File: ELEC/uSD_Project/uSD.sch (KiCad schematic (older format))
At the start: 5 parts, among them J1 CONN_01X08, U1 74HC595, U2 74HC165

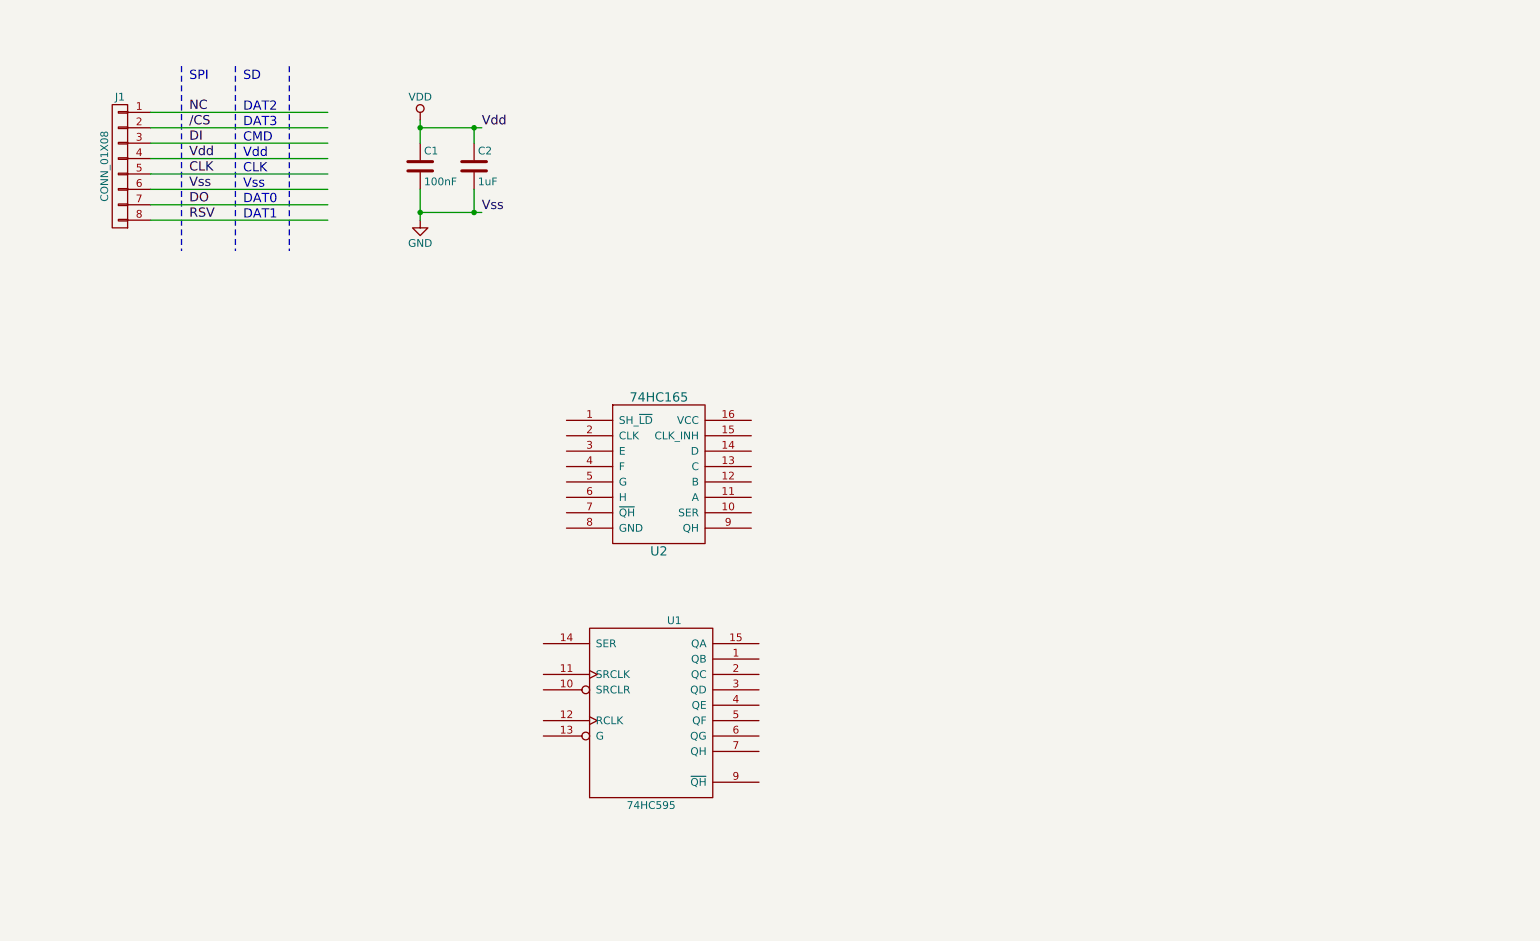
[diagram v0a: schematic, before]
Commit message: - Schematic capture - Creation of uSD part
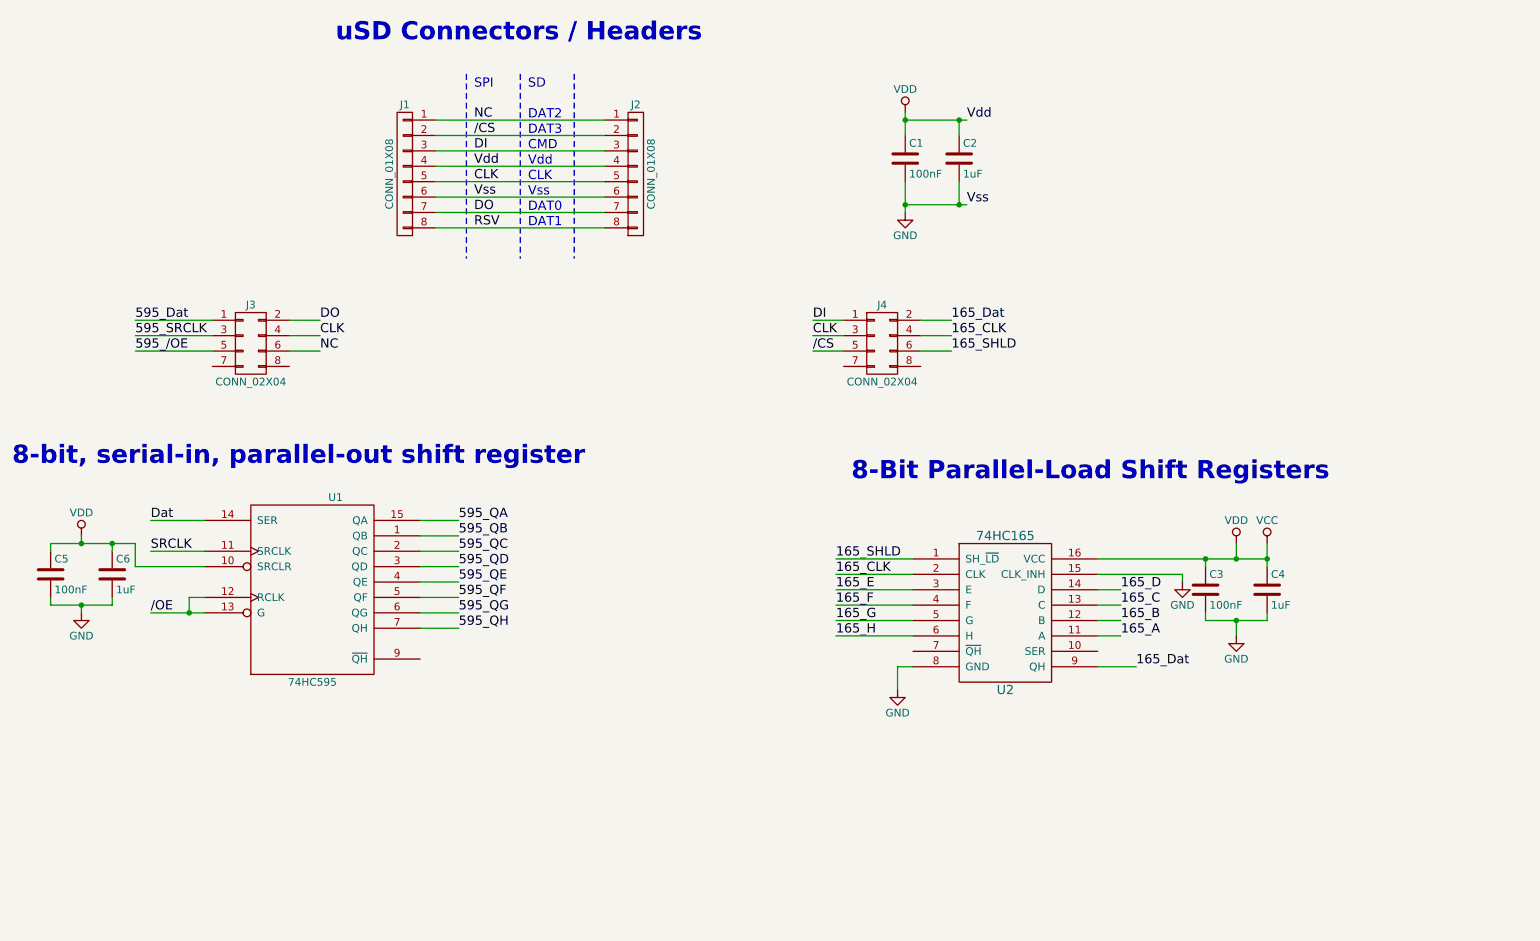
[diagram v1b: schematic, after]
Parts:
- added C3, C5: 100nF, Capacitors_SMD:C_0805_HandSoldering, symbol C
- added C4, C6: 1uF, Capacitors_SMD:C_0805_HandSoldering, symbol C
- added J2: CONN_01X08, Arranged_Pads.pretty:uSD, symbol CONN_01X08
- added J3, J4: CONN_02X04, symbol CONN_02X04
- U1: Digi PN (none) -> 296-38797-1-ND; Part Number (none) -> SN74HC595DBR
- U2: Digi PN (none) -> 296-23151-1-ND; Part Number (none) -> SN74HC165DBR
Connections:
- net labels added: /OE, 165_A, 165_B, 165_C, 165_CLK, 165_D, 165_Dat, 165_E, 165_F, 165_G, 165_H, 165_SHLD, 595_/OE, 595_Dat, 595_QA, 595_QB, 595_QC, 595_QD, 595_QE, 595_QF, 595_QG, 595_QH, 595_SRCLK, Dat, SRCLK, VCC
- wire segments 14 -> 72
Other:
- note added: "8-Bit Parallel-Load Shift Registers"
- note added: "8-bit, serial-in, parallel-out shift register"
- note added: "uSD Connectors / Headers"
- moved on the sheet: C1, C2, J1, U1, U2

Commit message: Added padi stamp to project, moved some parts around, added pin headers, fixed net labels for shift reg etc...
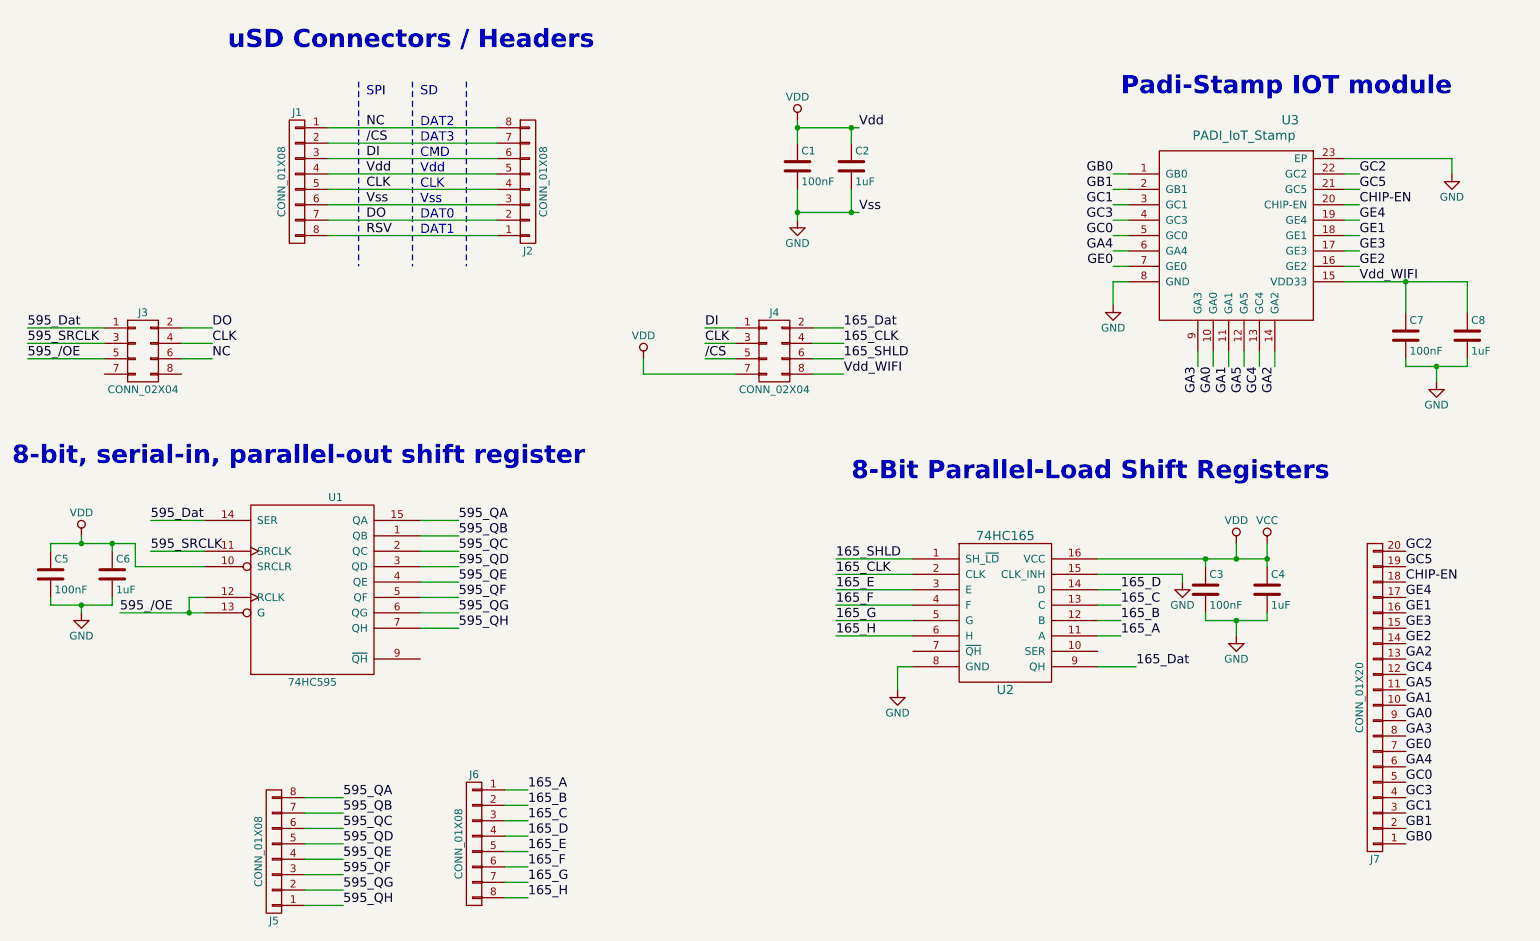
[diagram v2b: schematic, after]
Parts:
- added C7: 100nF, Capacitors_SMD:C_0805_HandSoldering, symbol C
- added C8: 1uF, Capacitors_SMD:C_0805_HandSoldering, symbol C
- added J5, J6: CONN_01X08, Pin_Headers:Pin_Header_Angled_1x08_Pitch1.27mm, symbol CONN_01X08
- added J7: CONN_01X20, Pin_Headers:Pin_Header_Angled_1x20_Pitch1.27mm, symbol CONN_01X20
- added U3: PADI_IoT_Stamp, modules:PADI_IoT_Stamp, symbol PADI_IoT_Stamp
- J1: footprint Pin_Headers:Pin_Header_Angled_1x08_Pitch1.27mm -> Pin_Headers:Pin_Header_Straight_1x08_Pitch1.27mm
- J3, J4: footprint (none) -> Pin_Headers:Pin_Header_Straight_2x04_Pitch1.27mm
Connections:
- net /OE is gone; now on net 595_/OE: U1.12 (RCLK), U1.13 (G)
- net Dat is gone; now on net 595_Dat: U1.14 (SER)
- net SRCLK is gone; now on net 595_SRCLK: U1.11 (SRCLK)
- net /CS: now also J2.7 (P7); no longer J2.2 (P2)
- net 165_A: now also J6.1 (P1)
- net 165_B: now also J6.2 (P2)
- net 165_C: now also J6.3 (P3)
- net 165_D: now also J6.4 (P4)
- net 165_E: now also J6.5 (P5)
- net 165_F: now also J6.6 (P6)
- net 165_G: now also J6.7 (P7)
- net 165_H: now also J6.8 (P8)
- net 595_QA: now also J5.8 (P8)
- net 595_QB: now also J5.7 (P7)
- net 595_QC: now also J5.6 (P6)
- net 595_QD: now also J5.5 (P5)
- net 595_QE: now also J5.4 (P4)
- net 595_QF: now also J5.3 (P3)
- net 595_QG: now also J5.2 (P2)
- net 595_QH: now also J5.1 (P1)
- net CLK: now also J2.4 (P4); no longer J2.5 (P5)
- net DI: now also J2.6 (P6); no longer J2.3 (P3)
- net DO: now also J2.2 (P2); no longer J2.7 (P7)
- net GND: now also J2.3 (P3), C7.2, C8.2, U3.23 (EP), U3.8 (GND); no longer J2.6 (P6)
- net NC: now also J2.8 (P8); no longer J2.1 (P1)
- net RSV: now also J2.1 (P1); no longer J2.8 (P8)
- net VCC: now also J2.5 (P5), J4.7 (P7); no longer J2.4 (P4)
- net Vdd_WIFI: now reaches J4.8 (P8)
- net Vdd_WIFI: now also C7.1, C8.1, U3.15 (VDD33)
- new net CHIP-EN: J7.18 (P18), U3.20 (CHIP-EN)
- new net GA0: J7.9 (P9), U3.10 (GA0)
- new net GA1: J7.10 (P10), U3.11 (GA1)
- new net GA2: J7.13 (P13), U3.14 (GA2)
- new net GA3: J7.8 (P8), U3.9 (GA3)
- new net GA4: J7.6 (P6), U3.6 (GA4)
- new net GA5: J7.11 (P11), U3.12 (GA5)
- new net GB0: J7.1 (P1), U3.1 (GB0)
- new net GB1: J7.2 (P2), U3.2 (GB1)
- new net GC0: J7.5 (P5), U3.5 (GC0)
- new net GC1: J7.3 (P3), U3.3 (GC1)
- new net GC2: J7.20 (P20), U3.22 (GC2)
- new net GC3: J7.4 (P4), U3.4 (GC3)
- new net GC4: J7.12 (P12), U3.13 (GC4)
- new net GC5: J7.19 (P19), U3.21 (GC5)
- new net GE0: J7.7 (P7), U3.7 (GE0)
- new net GE1: J7.16 (P16), U3.18 (GE1)
- new net GE2: J7.14 (P14), U3.16 (GE2)
- new net GE3: J7.15 (P15), U3.17 (GE3)
- new net GE4: J7.17 (P17), U3.19 (GE4)
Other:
- note added: "Padi-Stamp IOT module"
- moved on the sheet: C1, C2, J1, J2, J3, J4

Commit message: Changed out shift registers, started and almost completed routing
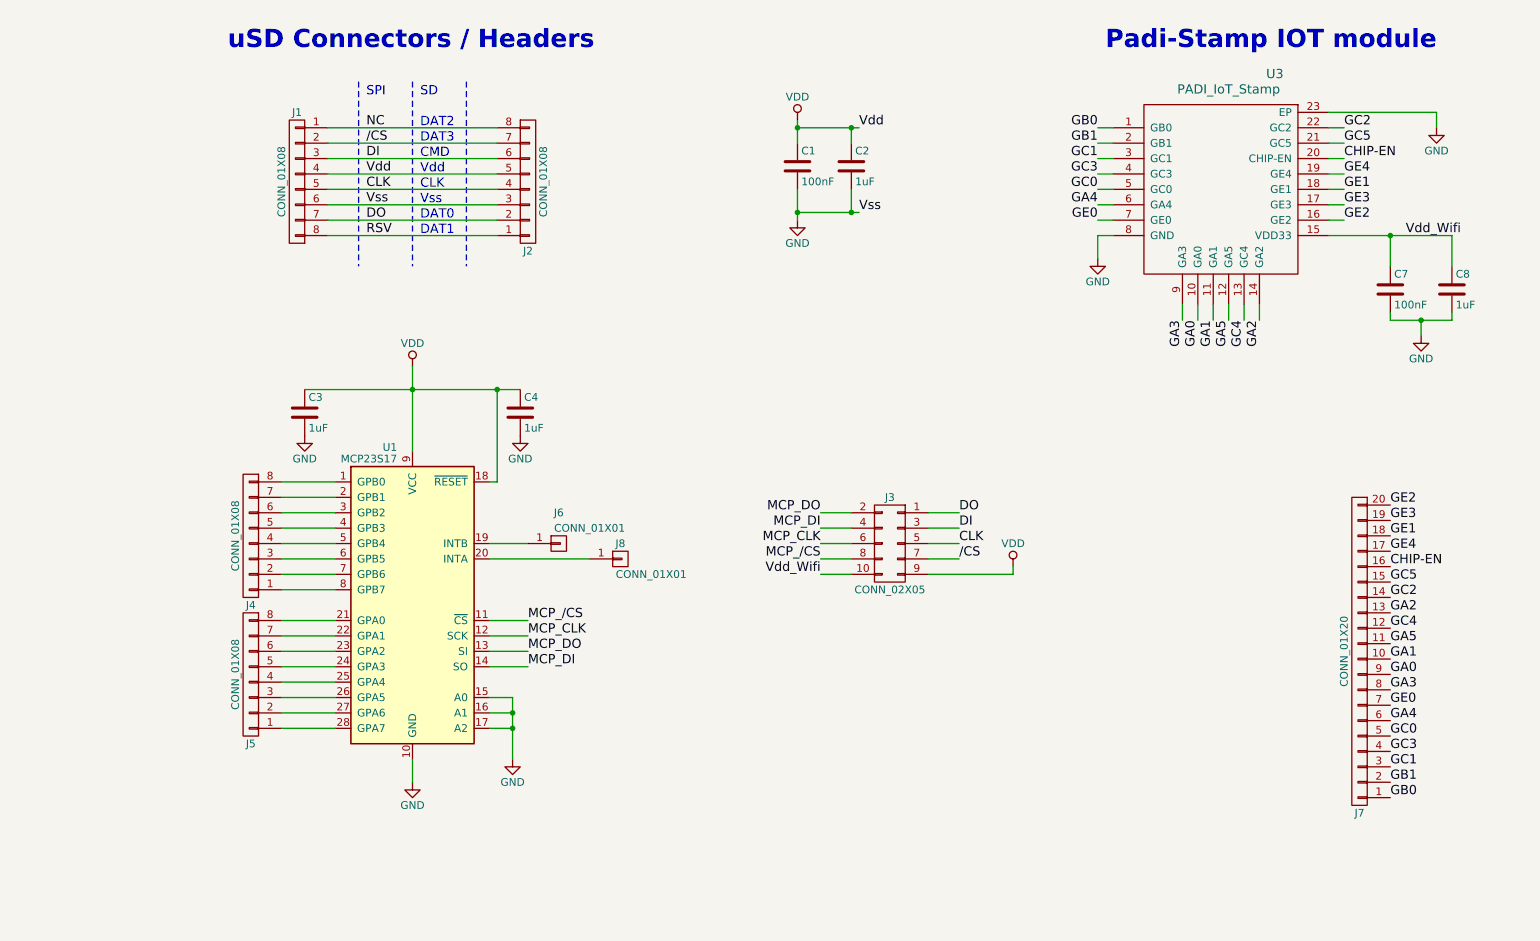
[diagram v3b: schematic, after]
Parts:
- removed C5: 100nF, Capacitors_SMD:C_0805_HandSoldering, symbol C
- removed C6: 1uF, Capacitors_SMD:C_0805_HandSoldering, symbol C
- removed J3, J4: CONN_02X04, Pin_Headers:Pin_Header_Straight_2x04_Pitch1.27mm, symbol CONN_02X04
- removed J6: CONN_01X08, Pin_Headers:Pin_Header_Angled_1x08_Pitch1.27mm, symbol CONN_01X08
- removed U1: 74HC595, Housings_SSOP.pretty:SSOP-16_4.4x5.2mm_Pitch0.65mm, symbol 74HC595
- removed U2: 74HC165, Housings_SSOP.pretty:SSOP-16_4.4x5.2mm_Pitch0.65mm, symbol 74HC165
- added J3: CONN_02X05, Pin_Headers:Pin_Header_Straight_2x05_Pitch1.27mm, symbol CONN_02X05
- added J4: CONN_01X08, Pin_Headers:Pin_Header_Angled_1x08_Pitch1.27mm, symbol CONN_01X08
- added J6, J8: CONN_01X01, Via:10mil_Via, symbol CONN_01X01
- added U1: MCP23S17, Housings_SSOP.pretty:SSOP-28_5.3x10.2mm_Pitch0.65mm, symbol MCP23S17
- C3: value 100nF -> 1uF
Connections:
- net /CS: now also J3.7 (P7)
- net CHIP-EN: now also J7.16 (P16); no longer J7.18 (P18)
- net CLK: now also J3.5 (P5)
- net DI: now also J3.3 (P3)
- net DO: now also J3.1 (P1)
- net GC2: now also J7.14 (P14); no longer J7.20 (P20)
- net GC5: now also J7.15 (P15); no longer J7.19 (P19)
- net GE1: now also J7.18 (P18); no longer J7.16 (P16)
- net GE2: now also J7.20 (P20); no longer J7.14 (P14)
- net GE3: now also J7.19 (P19); no longer J7.15 (P15)
- net GND: now also U1.10 (GND), U1.15 (A0), U1.16 (A1), U1.17 (A2)
- net 595_QA: no longer names the net of J5.8 (P8)
- net 595_QA: now also U1.21 (GPA0)
- net 595_QB: no longer names the net of J5.7 (P7)
- net 595_QB: now also U1.22 (GPA1)
- net 595_QC: no longer names the net of J5.6 (P6)
- net 595_QC: now also U1.23 (GPA2)
- net 595_QD: no longer names the net of J5.5 (P5)
- net 595_QD: now also U1.24 (GPA3)
- net 595_QE: no longer names the net of J5.4 (P4)
- net 595_QE: now also U1.25 (GPA4)
- net 595_QF: no longer names the net of J5.3 (P3)
- net 595_QF: now also U1.26 (GPA5)
- net 595_QG: no longer names the net of J5.2 (P2)
- net 595_QG: now also U1.27 (GPA6)
- net 595_QH: no longer names the net of J5.1 (P1)
- net 595_QH: now also U1.28 (GPA7)
- net VCC renamed VDD
- net VDD: now also J3.9 (P9), U1.18 (~RESET), U1.9 (VCC)
- net Vdd_WIFI renamed Vdd_Wifi
- net Vdd_Wifi: now also J3.10 (P10)
- new net: J4.8 (P8), U1.1 (GPB0)
- new net: J6.1 (P1), U1.19 (INTB)
- new net: J4.7 (P7), U1.2 (GPB1)
- new net: J8.1 (P1), U1.20 (INTA)
- new net: J4.6 (P6), U1.3 (GPB2)
- new net: J4.5 (P5), U1.4 (GPB3)
- new net: J4.4 (P4), U1.5 (GPB4)
- new net: J4.3 (P3), U1.6 (GPB5)
- new net: J4.2 (P2), U1.7 (GPB6)
- new net: J4.1 (P1), U1.8 (GPB7)
- new net MCP_/CS: J3.8 (P8), U1.11 (~CS)
- new net MCP_CLK: J3.6 (P6), U1.12 (SCK)
- new net MCP_DI: J3.4 (P4), U1.14 (SO)
- new net MCP_DO: J3.2 (P2), U1.13 (SI)
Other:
- note removed: "8-Bit Parallel-Load Shift Registers"
- note removed: "8-bit, serial-in, parallel-out shift register"
- moved on the sheet: C7, C8, J7, U3
